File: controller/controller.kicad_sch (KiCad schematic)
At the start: 6 parts, among them J1 USB-C 5V, J3 IEC C14, J4 Cooktop

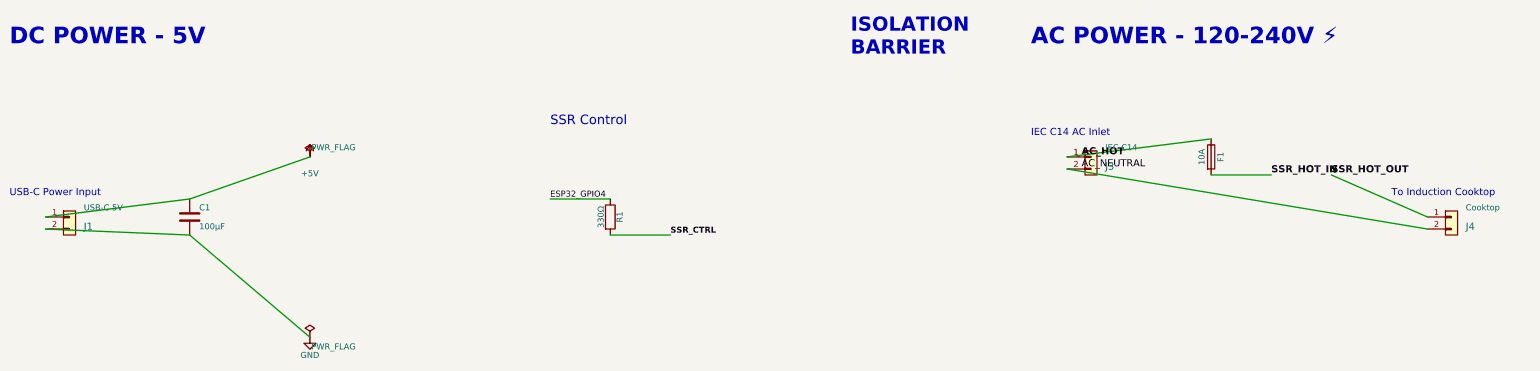
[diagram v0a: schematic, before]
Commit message: Add controller symbols and docs
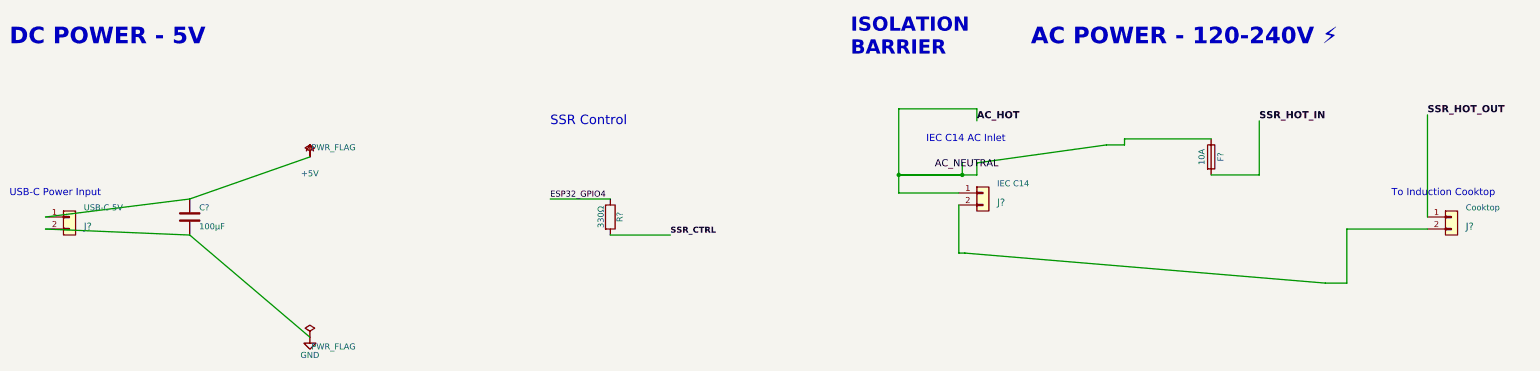
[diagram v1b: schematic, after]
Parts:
- renumbered C1 to C?, F1 to F?, J1 to J?, J3 to J?, J4 to J?, R1 to R?
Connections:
- net AC_HOT: now also F?.1, J?.1 (Pin_1)
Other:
- moved on the sheet: J?
